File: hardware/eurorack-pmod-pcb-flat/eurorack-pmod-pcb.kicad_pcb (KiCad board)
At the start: 2 copper layers, 40 x 110 mm, 102 parts, among them J1 EURORACK_PWR, J10 PJ398SM, J2 PMOD, J3 PJ398SM, J4 PJ398SM, J5 PJ398SM, J6 PJ398SM, J7 PJ398SM, J8 PJ398SM, J9 PJ398SM, U1 LM4040DBZ-3, U2 TL072, U3 AK4619VN, U4 TL074, U5 TL074, U6 TL074, U7 TL074

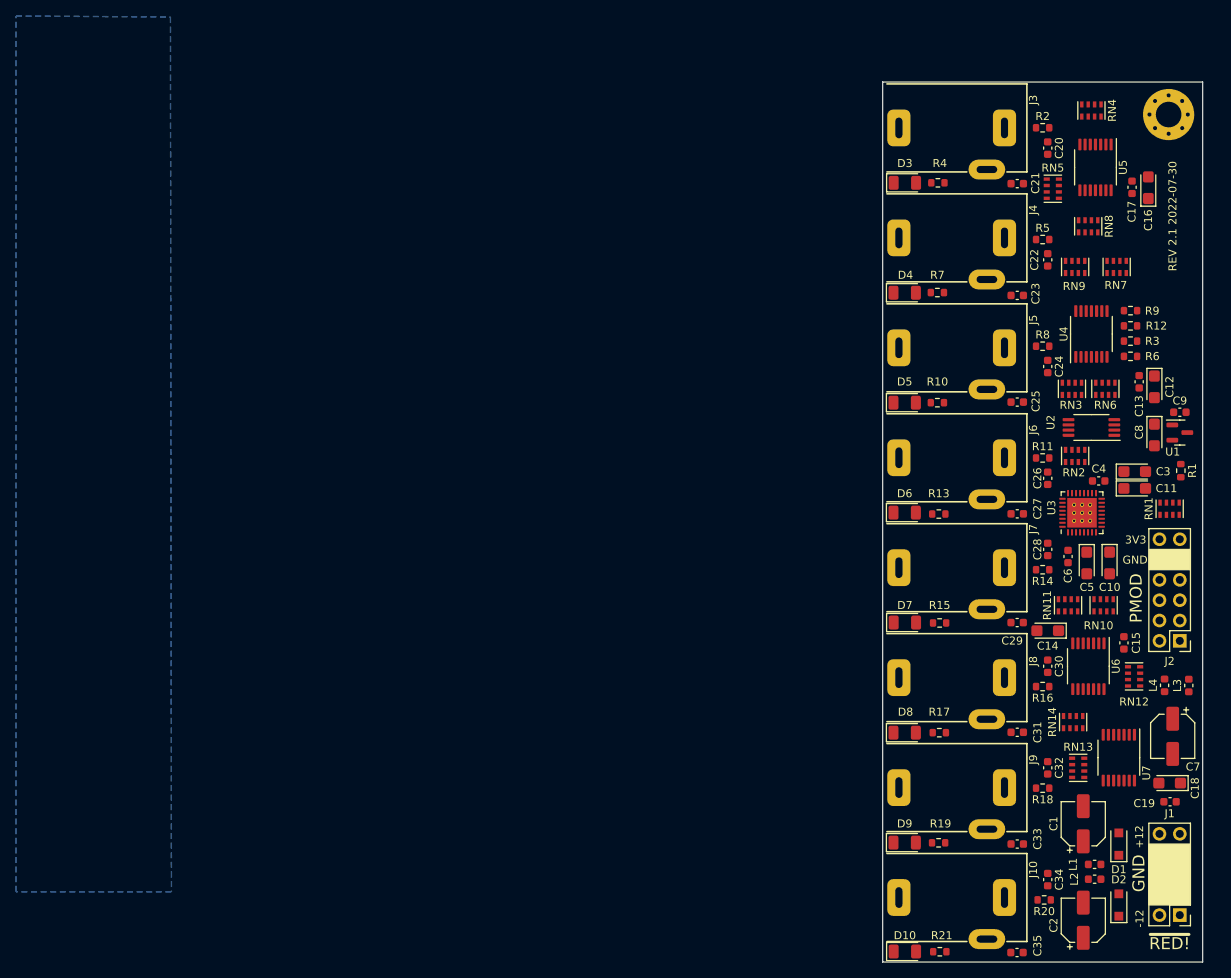
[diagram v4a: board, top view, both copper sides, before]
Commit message: rev2-flat: route all power and vref
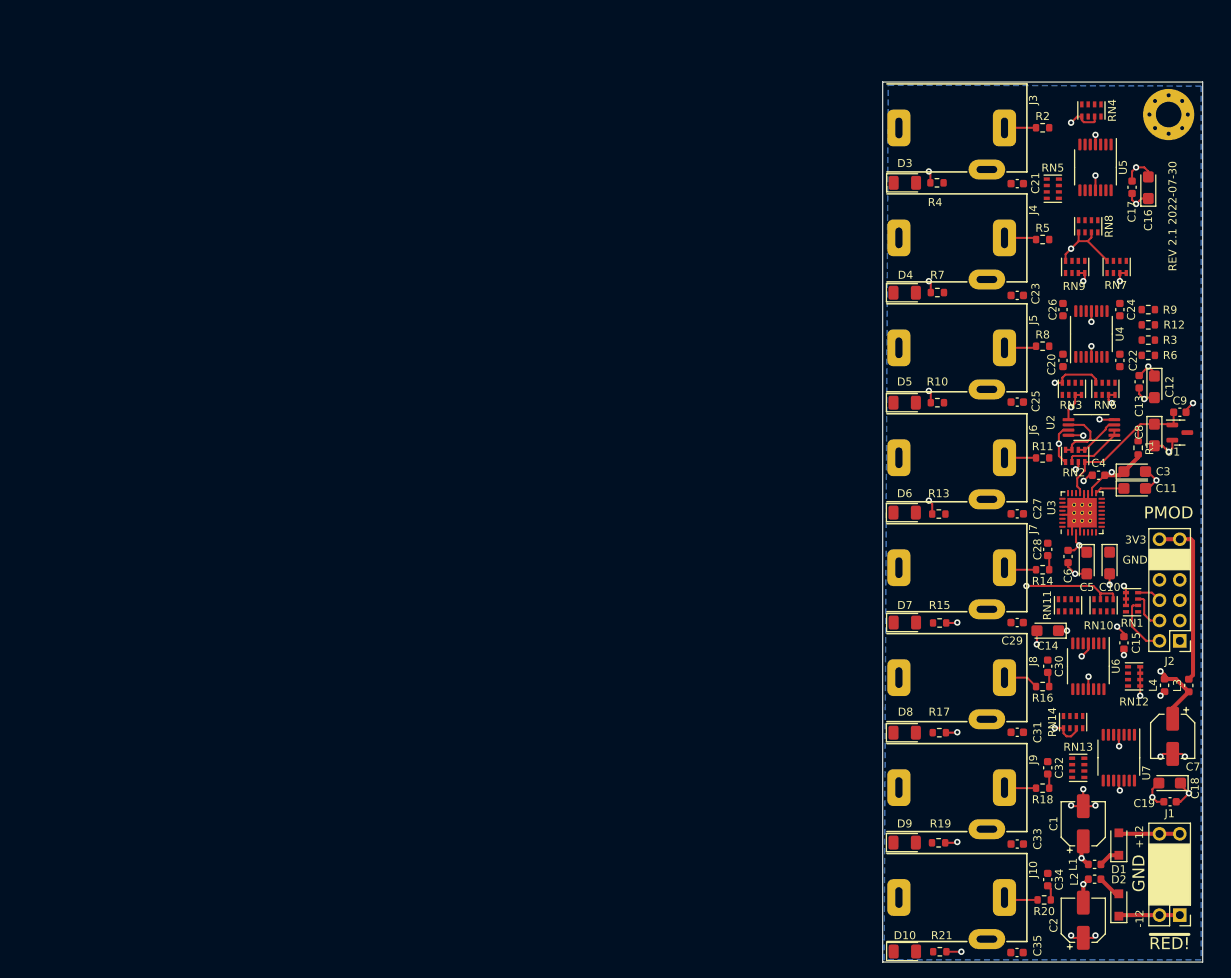
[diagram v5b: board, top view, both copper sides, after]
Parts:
- moved C20 26.6 mm to (2.54, 34.8), turned to 90 degrees
- moved C26 21.2 mm to (2.54, 28.4)
- moved C22 15.5 mm to (9.65, 34.8), turned to 90 degrees
- moved RN1 12.6 mm to (11.2, 65.0), turned to 180 degrees
- moved C24 11.5 mm to (9.65, 28.4)
- moved R1 6.05 mm to (11.9, 45.7)
- moved R12 2.23 mm to (13.2, 30.4)
- moved R3 2.23 mm to (13.2, 32.3)
- moved R6 2.23 mm to (13.2, 34.2)
- moved R9 2.23 mm to (13.2, 28.4)
- moved C4 0.71 mm to (6.99, 49.1)
- moved R4 0.11 mm to (-13.2, 12.6), turned to 0 degrees
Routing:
- net +12V: track 0.00 -> 134.6 mm, vias 0 -> 9
- net -12V: track 0.00 -> 132.7 mm, vias 0 -> 8
- net /-VCOM: track 0.00 -> 125.9 mm, vias 0 -> 6
- net GND: track 0.00 -> 81.3 mm, vias 0 -> 32
- net +3.3VA: track 0.00 -> 41.8 mm, vias 0 -> 2
- net VDD: track 0.00 -> 37.6 mm, vias 0 -> 3
- net Net-(J2-Pad11): track 0.00 -> 21.8 mm
- net /VREFH: track 0.00 -> 21.0 mm
- net Net-(RN2-Pad3): track 0.00 -> 8.03 mm
- net Net-(RN2-Pad6): track 0.00 -> 7.70 mm
- net Net-(D2-Pad1): track 0.00 -> 7.68 mm
- net Net-(D1-Pad2): track 0.00 -> 7.67 mm
- net /SCL: track 0.00 -> 7.50 mm
- net Net-(RN2-Pad1): track 0.00 -> 5.90 mm
- net /SDA: track 0.00 -> 4.83 mm
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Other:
- copper layers 2 -> 4

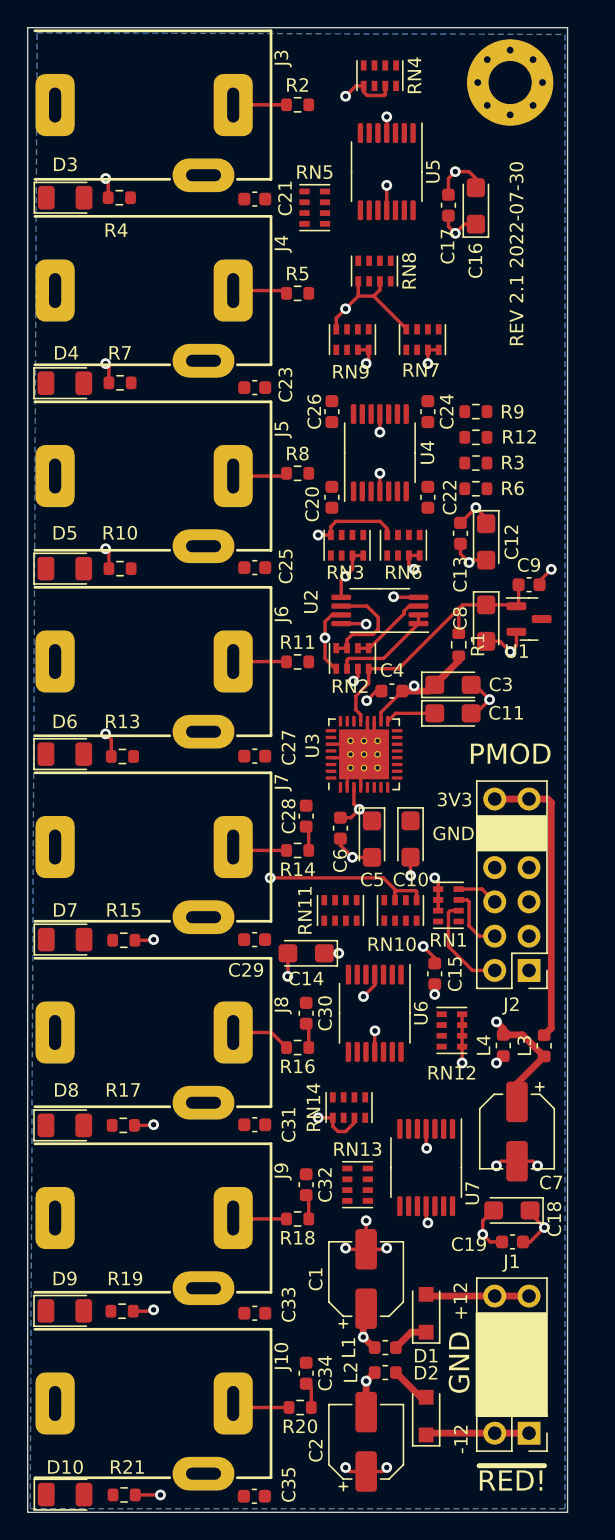
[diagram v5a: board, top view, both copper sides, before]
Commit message: rev2-flat: start routing signal traces
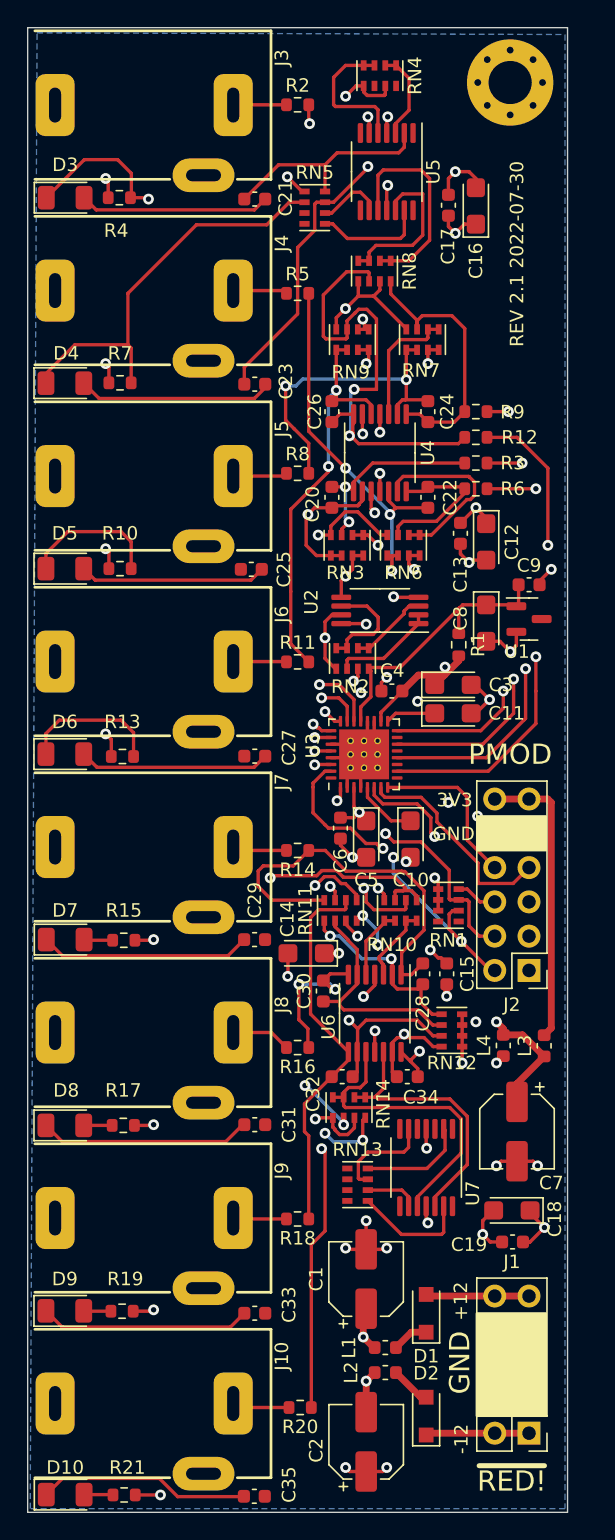
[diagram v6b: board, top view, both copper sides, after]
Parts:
- moved C34 23.2 mm to (8.13, 77.7), turned to 0 degrees
- moved C28 14.5 mm to (9.27, 70.1), turned to 90 degrees
- moved C32 8.43 mm to (3.30, 77.7), turned to 180 degrees
- moved C30 2.08 mm to (1.91, 71.4), turned to 90 degrees
- moved C15 0.89 mm to (11.0, 70.1)
- moved C5 0.43 mm to (5.08, 60.1)
- moved C25 0.28 mm to (-3.43, 40.1), turned to 0 degrees
- moved C23 0.25 mm to (-3.17, 26.4)
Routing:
- net Net-(C34-Pad2): track 1.92 -> 58.5 mm, vias 0 -> 3
- net Net-(C20-Pad1): track 0.00 -> 41.5 mm, vias 0 -> 2
- net Net-(C26-Pad2): track 0.00 -> 38.3 mm, vias 0 -> 2
- net /dual_mono_outputs2/OUT2: track 0.00 -> 37.7 mm, vias 0 -> 3
- net /dual_mono_inputs2/IN1_3V: track 0.00 -> 37.7 mm, vias 0 -> 2
- net /dual_mono_inputs2/IN2_3V: track 0.00 -> 36.9 mm, vias 0 -> 2
- net /dual_mono_outputs2/OUT1: track 0.00 -> 35.2 mm, vias 0 -> 3
- net /SDOUT1: track 0.00 -> 33.9 mm, vias 0 -> 2
- net /dual_mono_inputs1/IN2_3V: track 0.00 -> 31.4 mm, vias 0 -> 2
- net /dual_mono_inputs1/IN1_3V: track 0.00 -> 30.6 mm, vias 0 -> 2
- net Net-(C26-Pad1): track 0.00 -> 30.6 mm, vias 0 -> 2
- net Net-(D4-Pad1): track 0.00 -> 30.3 mm
- net Net-(C22-Pad1): track 0.00 -> 29.7 mm, vias 0 -> 3
- net /PDN: track 3.06 -> 32.1 mm, vias 0 -> 3
- net Net-(C28-Pad2): track 1.84 -> 29.5 mm
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
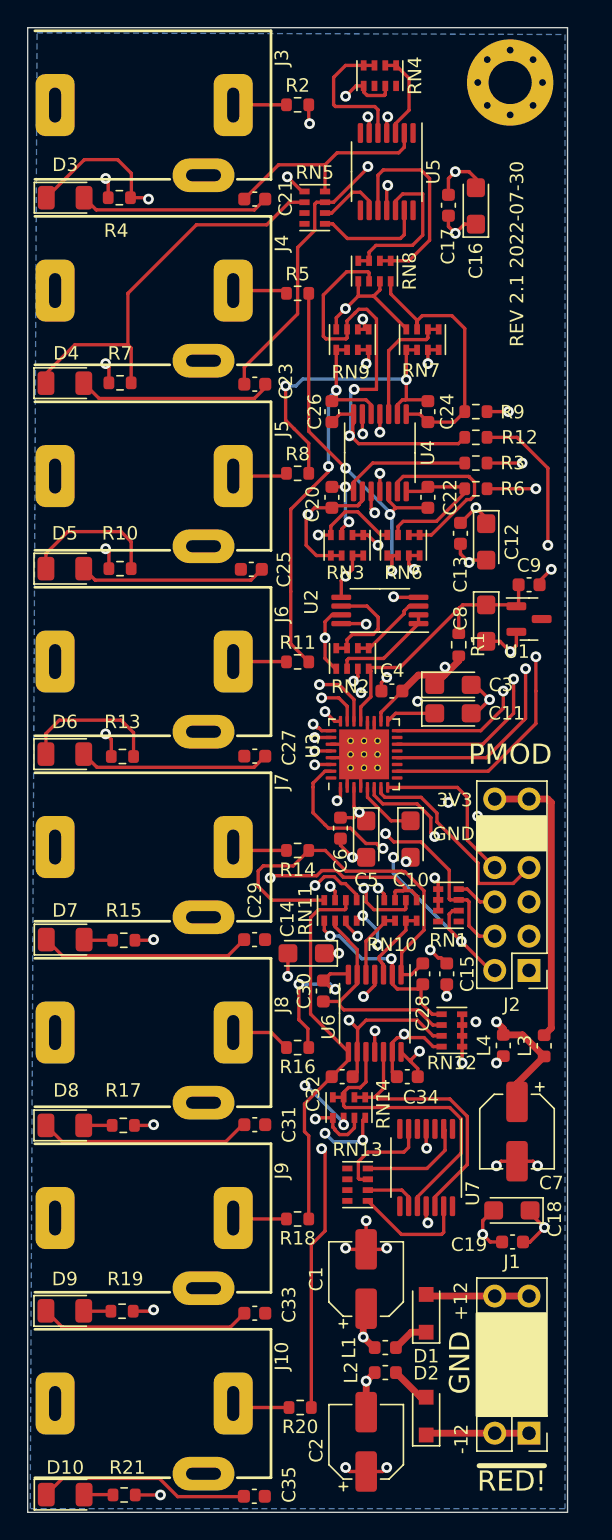
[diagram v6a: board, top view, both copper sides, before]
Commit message: rev2-flat: all signals routed and DRC passes
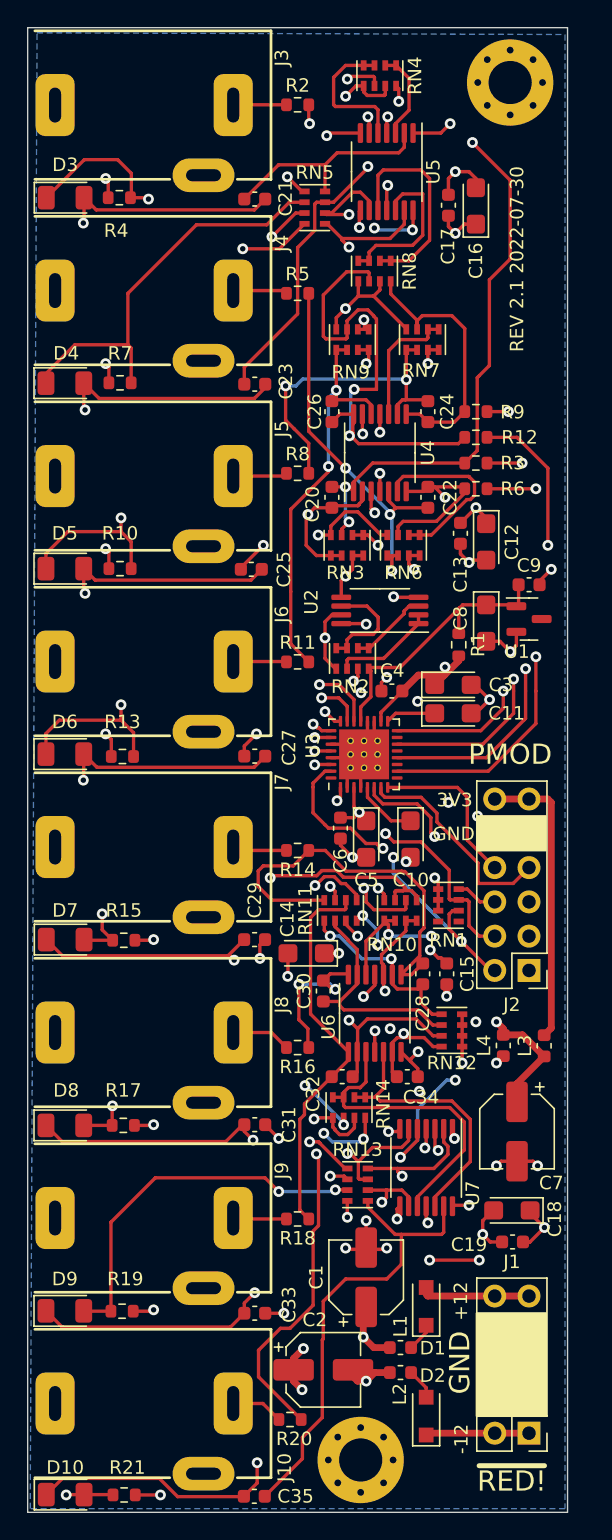
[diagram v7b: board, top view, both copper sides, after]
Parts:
- added REF**: MountingHole_3.2mm_M3_Pad_Via, MountingHole:MountingHole_3.2mm_M3_Pad_Via, F.Cu at (4.67, 106.1)
- added REF**: OSHW-Logo2_9.8x8mm_SilkScreen, Symbol:OSHW-Logo2_9.8x8mm_SilkScreen, B.Cu at (13.2, 79.9)
- moved C2 6.21 mm to (1.91, 99.4), turned to 0 degrees
- moved R20 1.16 mm to (-0.56, 103.1)
- moved L1 1.12 mm to (7.62, 97.8)
- moved L2 1.12 mm to (7.62, 99.6)
- moved D1 0.51 mm to (9.53, 94.7)
- moved C1 0.13 mm to (5.08, 92.6)
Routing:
- net Net-(C27-Pad2): track 14.2 -> 76.6 mm, vias 0 -> 3
- net Net-(C22-Pad2): track 11.4 -> 65.0 mm, vias 0 -> 2
- net Net-(C29-Pad2): track 15.7 -> 67.8 mm, vias 0 -> 4
- net Net-(C25-Pad2): track 13.9 -> 62.5 mm, vias 0 -> 2
- net Net-(C21-Pad2): track 14.1 -> 60.0 mm, vias 0 -> 2
- net Net-(D6-Pad1): track 10.6 -> 55.8 mm, vias 0 -> 2
- net Net-(C27-Pad1): track 8.25 -> 51.0 mm, vias 0 -> 2
- net Net-(C29-Pad1): track 7.90 -> 49.7 mm, vias 0 -> 2
- net Net-(C23-Pad2): track 14.2 -> 53.7 mm, vias 0 -> 2
- net Net-(D10-Pad2): track 2.15 -> 38.0 mm, vias 0 -> 2
- net Net-(C20-Pad2): track 15.2 -> 49.4 mm, vias 2 -> 4
- net Net-(C25-Pad1): track 4.87 -> 37.8 mm, vias 0 -> 2
- net Net-(D5-Pad1): track 10.4 -> 42.6 mm, vias 0 -> 2
- net Net-(C35-Pad2): track 15.7 -> 47.2 mm, vias 0 -> 2
- net Net-(D7-Pad2): track 2.14 -> 32.9 mm, vias 0 -> 2
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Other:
- board text added: "3V3_IN"
- board text added: "BICK"
- board text added: "CC-BY-SA 4.0"
- board text added: "IN1"
- board text added: "IN2"
- board text added: "IN3"
- board text added: "IN4"
- board text added: "LRCK"
- board text added: "MCLK"
- board text added: "OUT1"
- board text added: "OUT2"
- board text added: "OUT3"
- board text added: "OUT4"
- board text added: "PDN"
- board text added: "SCL"
- board text added: "SDA"
- board text added: "SDI"
- board text added: "SDO"
- board text added: "sebholzapfel.com"
